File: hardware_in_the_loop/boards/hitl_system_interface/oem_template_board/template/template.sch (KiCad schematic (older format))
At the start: 35 parts, among them J1 CONN_02X03, U1 MCP2561-E_SN, U101 TPS560430YF, U2 ATMEGA16M1, Y1 Crystal_SMD

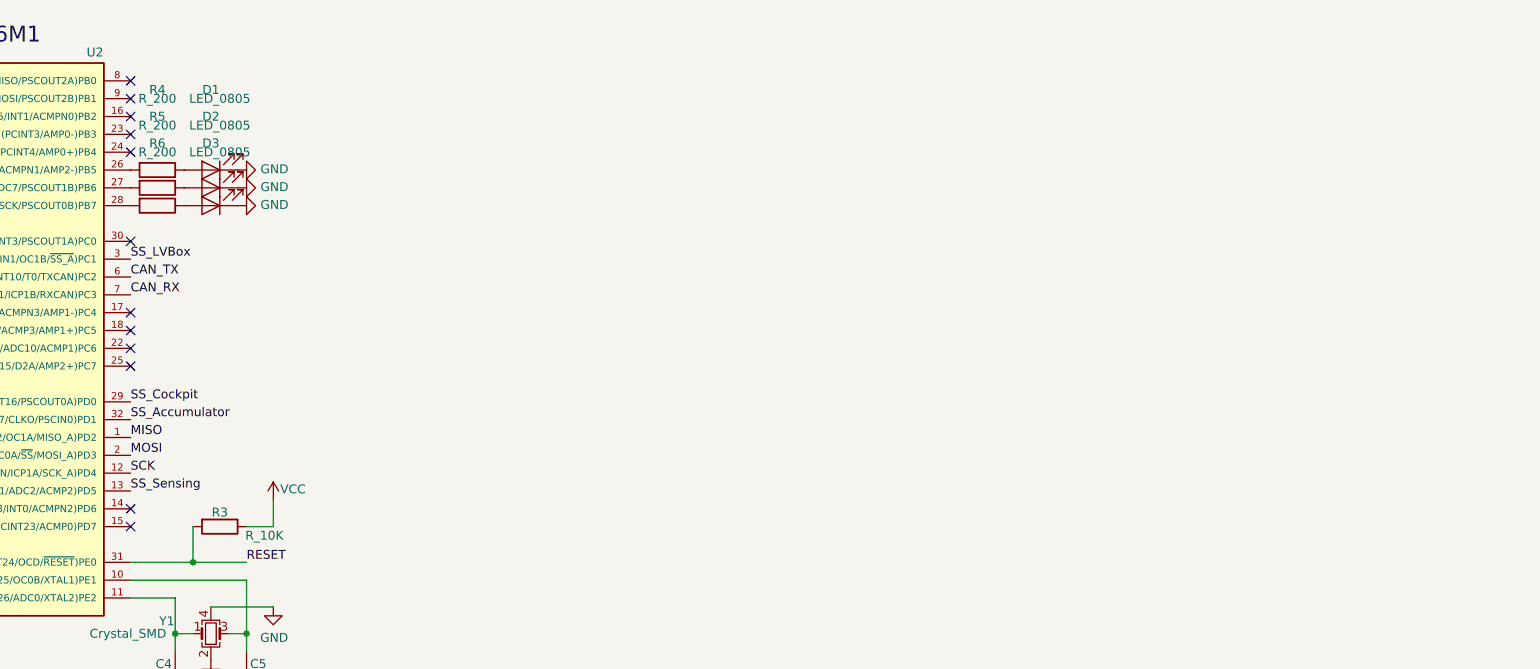
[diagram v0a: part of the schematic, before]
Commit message: Worked on USB_MicroB connections to FT232R
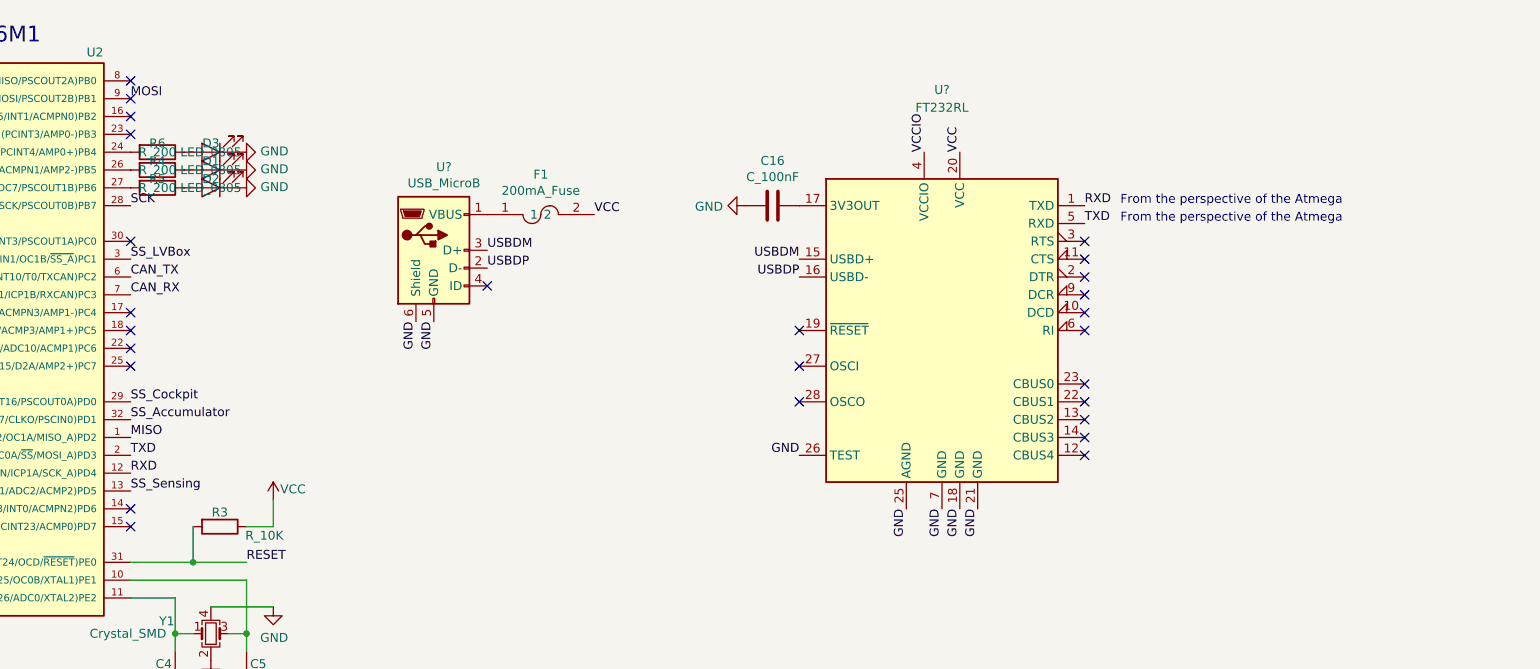
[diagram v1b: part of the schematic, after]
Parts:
- added C16: C_100nF, footprints:C_0603_1608Metric, symbol formula:C_100nF
- added F1: 200mA_Fuse, footprints:Fuse_1812, symbol formula:200mA_Fuse
- added U?: FT232RL, Package_SO:SSOP-28_5.3x10.2mm_P0.65mm, symbol formula:FT232RL
- added U?: USB_MicroB, Connectors_USB:USB_Micro-B_Molex-105017-0001, symbol formula:USB_MicroB
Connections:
- net GND: now also C16.2, U?.18 (GND), U?.21 (GND), U?.25 (AGND), U?.26 (TEST), U?.5 (GND), U?.6 (Shield), U?.7 (GND)
- net MOSI: now also U2.9 ((PCINT1/MOSI/PSCOUT2B)PB1); no longer U2.2 ((PCINT19/TXD/TXLIN/OC0A/~SS~/MOSI_A)PD3)
- net SCK: now also U2.28 ((PCINT7/ADC4/SCK/PSCOUT0B)PB7); no longer U2.12 ((PCINT20/ADC1/RXD/RXLIN/ICP1A/SCK_A)PD4)
- net VCC: now also F1.2, U?.20 (VCC)
- net at U2.24 ((PCINT4/AMP0+)PB4): now also R6.2
- new net: C16.1, U?.17 (3V3OUT)
- new net: F1.1, U?.1 (VBUS)
- new net RXD: U2.12 ((PCINT20/ADC1/RXD/RXLIN/ICP1A/SCK_A)PD4), U?.1 (TXD)
- new net TXD: U2.2 ((PCINT19/TXD/TXLIN/OC0A/~SS~/MOSI_A)PD3), U?.5 (RXD)
- new net USBDM: U?.15 (USBD+), U?.3 (D+)
- new net USBDP: U?.16 (USBD-), U?.2 (D-)
- new net VCCIO: U?.4 (VCCIO)
- no-connect marks 14 -> 28
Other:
- note added: "From the perspective of the Atmega"
- moved on the sheet: D3, R6
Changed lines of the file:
@@
 Text Label 3650 3000 0    50   ~ 0
 MISO
-Text Label 3650 3100 0    50   ~ 0
+Text Label 3650 1100 0    50   ~ 0
 MOSI
 Text Label 3650 3200 0    50   ~ 0
-SCK
+RXD
 Text Label 4300 3700 0    50   ~ 0
 RESET
@@
 U 1 1 5F9FF68D
 P 4100 1500
-F 0 "D1" H 4100 1050 50  0000 C CNN
-F 1 "LED_0805" H 4050 1100 50  0000 C CNN
+F 0 "D1" H 4100 1450 50  0000 C CNN
+F 1 "LED_0805" H 4100 1500 50  0000 C CNN
 F 2 "footprints:LED_0805_OEM" H 4000 1500 50  0001 C CNN
 F 3 "http://www.osram-os.com/Graphics/XPic9/00078860_0.pdf" H 4100 1600 50  0001 C CNN
@@
 U 1 1 5FA08DE6
 P 3800 1500
-F 0 "R4" V 3350 1500 50  0000 C CNN
-F 1 "R_200" V 3400 1500 50  0000 C CNN
+F 0 "R4" V 3750 1500 50  0000 C CNN
+F 1 "R_200" V 3800 1500 50  0000 C CNN
 F 2 "footprints:R_0805_OEM" H 3730 1500 50  0001 C CNN
 F 3 "https://www.seielect.com/Catalog/SEI-RMCF_RMCP.pdf" H 3880 1500 50  0001 C CNN
@@
 U 1 1 5FA12380
 P 4100 1600
-F 0 "D2" H 4100 1200 50  0000 C CNN
-F 1 "LED_0805" H 4050 1250 50  0000 C CNN
+F 0 "D2" H 4100 1550 50  0000 C CNN
+F 1 "LED_0805" H 4100 1600 50  0000 C CNN
 F 2 "footprints:LED_0805_OEM" H 4000 1600 50  0001 C CNN
 F 3 "http://www.osram-os.com/Graphics/XPic9/00078860_0.pdf" H 4100 1700 50  0001 C CNN
@@
 U 1 1 5FA12389
 P 3800 1600
-F 0 "R5" V 3400 1600 50  0000 C CNN
-F 1 "R_200" V 3450 1600 50  0000 C CNN
+F 0 "R5" V 3750 1600 50  0000 C CNN
+F 1 "R_200" V 3800 1600 50  0000 C CNN
 F 2 "footprints:R_0805_OEM" H 3730 1600 50  0001 C CNN
 F 3 "https://www.seielect.com/Catalog/SEI-RMCF_RMCP.pdf" H 3880 1600 50  0001 C CNN
@@
 $EndComp
 $Comp
-L formula:LED_0805 D3
-U 1 1 5FA147E9
-P 4100 1700
-F 0 "D3" H 4100 1350 50  0000 C CNN
-F 1 "LED_0805" H 4050 1400 50  0000 C CNN
-F 2 "footprints:LED_0805_OEM" H 4000 1700 50  0001 C CNN
-F 3 "http://www.osram-os.com/Graphics/XPic9/00078860_0.pdf" H 4100 1800 50  0001 C CNN
-F 4 "DK" H 4100 1700 60  0001 C CNN "MFN"
-F 5 "475-1410-1-ND" H 4100 1700 60  0001 C CNN "MPN"
-F 6 "https://www.digikey.com/products/en?keywords=475-1410-1-ND" H 4500 2200 60  0001 C CNN "PurchasingLink"
-	1    4100 1700
-	-1   0    0    1
-$EndComp
-$Comp
 L formula:R_200 R6
 U 1 1 5FA147F2
-P 3800 1700
-F 0 "R6" V 3450 1700 50  0000 C CNN
-F 1 "R_200" V 3500 1700 50  0000 C CNN
-F 2 "footprints:R_0805_OEM" H 3730 1700 50  0001 C CNN
-F 3 "https://www.seielect.com/Catalog/SEI-RMCF_RMCP.pdf" H 3880 1700 50  0001 C CNN
-F 4 "DK" H 3800 1700 60  0001 C CNN "MFN"
-F 5 "RMCF0805JT200RCT-ND" H 3800 1700 60  0001 C CNN "MPN"
-F 6 "https://www.digikey.com/products/en?keywords=RMCF0805JT200RCT-ND" H 4280 2100 60  0001 C CNN "PurchasingLink"
-	1    3800 1700
+P 3800 1400
+F 0 "R6" V 3750 1400 50  0000 C CNN
+F 1 "R_200" V 3800 1400 50  0000 C CNN
+F 2 "footprints:R_0805_OEM" H 3730 1400 50  0001 C CNN
+F 3 "https://www.seielect.com/Catalog/SEI-RMCF_RMCP.pdf" H 3880 1400 50  0001 C CNN
+F 4 "DK" H 3800 1400 60  0001 C CNN "MFN"
+F 5 "RMCF0805JT200RCT-ND" H 3800 1400 60  0001 C CNN "MPN"
+F 6 "https://www.digikey.com/products/en?keywords=RMCF0805JT200RCT-ND" H 4280 1800 60  0001 C CNN "PurchasingLink"
+	1    3800 1400
 	0    1    1    0
 $EndComp
@@
 L power:GND #PWR021
 U 1 1 5FA147F8
-P 4250 1700
-F 0 "#PWR021" H 4250 1450 50  0001 C CNN
-F 1 "GND" V 4255 1572 50  0000 R CNN
-F 2 "" H 4250 1700 50  0001 C CNN
-F 3 "" H 4250 1700 50  0001 C CNN
-	1    4250 1700
+P 4250 1400
+F 0 "#PWR021" H 4250 1150 50  0001 C CNN
+F 1 "GND" V 4255 1272 50  0000 R CNN
+F 2 "" H 4250 1400 50  0001 C CNN
+F 3 "" H 4250 1400 50  0001 C CNN
+	1    4250 1400
 	0    -1   -1   0
 $EndComp
@@
 NoConn ~ 3650 1200
 NoConn ~ 3650 1300
-NoConn ~ 3650 1400
-NoConn ~ 3650 1900
 NoConn ~ 3650 2300
 NoConn ~ 3650 2400
@@
 NoConn ~ 3650 3400
 NoConn ~ 3650 3500
+$Comp
+L formula:LED_0805 D3
+U 1 1 5FA147E9
+P 4100 1400
+F 0 "D3" H 4100 1350 50  0000 C CNN
+F 1 "LED_0805" H 4100 1400 50  0000 C CNN
+F 2 "footprints:LED_0805_OEM" H 4000 1400 50  0001 C CNN
+F 3 "http://www.osram-os.com/Graphics/XPic9/00078860_0.pdf" H 4100 1500 50  0001 C CNN
+F 4 "DK" H 4100 1400 60  0001 C CNN "MFN"
+F 5 "475-1410-1-ND" H 4100 1400 60  0001 C CNN "MPN"
+F 6 "https://www.digikey.com/products/en?keywords=475-1410-1-ND" H 4500 1900 60  0001 C CNN "PurchasingLink"
+	1    4100 1400
+	-1   0    0    1
+$EndComp
+Text Label 3650 3100 0    50   ~ 0
+TXD
+Text Label 3650 1700 0    50   ~ 0
+SCK
+NoConn ~ 3650 1900
+Text Label 9000 1800 0    50   ~ 0
+TXD
+Text Label 9000 1700 0    50   ~ 0
+RXD
+Text Notes 9200 1700 0    50   ~ 0
+From the perspective of the Atmega
+Text Notes 9200 1800 0    50   ~ 0
+From the perspective of the Atmega
+NoConn ~ 9000 1900
+NoConn ~ 9000 2000
+Text Label 8000 3400 3    50   ~ 0
+GND
+Text Label 8200 3400 3    50   ~ 0
+GND
+Text Label 8300 3400 3    50   ~ 0
+GND
+Text Label 8400 3400 3    50   ~ 0
+GND
+Text Label 7400 3100 2    50   ~ 0
+GND
+NoConn ~ 9000 2700
+NoConn ~ 9000 2800
+NoConn ~ 9000 2900
+NoConn ~ 9000 3000
+NoConn ~ 9000 3100
+NoConn ~ 9000 2400
+NoConn ~ 9000 2300
+NoConn ~ 9000 2200
+NoConn ~ 9000 2100
+$Comp
+L formula:C_100nF C16
+U 1 1 5FA17A78
+P 7250 1700
+F 0 "C16" V 6998 1700 50  0000 C CNN
+F 1 "C_100nF" V 7089 1700 50  0000 C CNN
+F 2 "footprints:C_0603_1608Metric" H 7288 1550 50  0001 C CNN
+F 3 "http://www.samsungsem.com/kr/support/product-search/mlcc/CL10A475KQ8NNNC.jsp" H 7275 1800 50  0001 C CNN
+F 4 "DK" H 7250 1700 60  0001 C CNN "MFN"
+F 5 "1276-6717-1-ND" H 7250 1700 60  0001 C CNN "MPN"
+F 6 "https://www.digikey.com/product-detail/en/samsung-electro-mechanics/CL10B104KA8WPNC/1276-6717-1-ND/5961576" H 7675 2200 60  0001 C CNN "PurchasingLink"
+	1    7250 1700
+	0    1    1    0
+$EndComp
+$Comp
+L power:GND #PWR?
+U 1 1 5FA19E14
+P 7100 1700
+F 0 "#PWR?" H 7100 1450 50  0001 C CNN
+F 1 "GND" V 7105 1572 50  0000 R CNN
+F 2 "" H 7100 1700 50  0001 C CNN
+F 3 "" H 7100 1700 50  0001 C CNN
+	1    7100 1700
+	0    1    1    0
+$EndComp
+$Comp
+L formula:USB_MicroB U?
+U 1 1 5FA24431
+P 5350 1950
+F 0 "U?" H 5407 2417 50  0000 C CNN
+F 1 "USB_MicroB" H 5407 2326 50  0000 C CNN
+F 2 "Connectors_USB:USB_Micro-B_Molex-105017-0001" H 5300 2300 50  0001 C CNN
+F 3 "https://www.molex.com/pdm_docs/sd/1050170001_sd.pdf" H 5300 2300 50  0001 C CNN
+F 4 "DK" H 5600 1700 50  0001 C CNN "MFN"
+F 5 "WM1399CT-ND" H 5700 1800 50  0001 C CNN "MPN"
+F 6 "https://www.digikey.com/product-detail/en/molex-llc/1050170001/WM1399CT-ND/2350885" H 5800 1900 50  0001 C CNN "PurchasingLink"
+	1    5350 1950
+	1    0    0    -1
+$EndComp
+Text Label 5350 2350 3    50   ~ 0
+GND
+Text Label 5250 2350 3    50   ~ 0
+GND
+NoConn ~ 5650 2150
+$Comp
+L formula:FT232RL U?
+U 1 1 5F9FAF59
+P 8200 2400
+F 0 "U?" H 8200 3750 50  0000 C CNN
+F 1 "FT232RL" H 8200 3650 50  0000 C CNN
+F 2 "Package_SO:SSOP-28_5.3x10.2mm_P0.65mm" H 9300 1500 50  0001 C CNN
+F 3 "https://www.ftdichip.com/Support/Documents/DataSheets/ICs/DS_FT232R.pdf" H 8200 2400 50  0001 C CNN
+F 4 "https://www.digikey.com/product-detail/en/ftdi-future-technology-devices-international-ltd/FT232RL-REEL/768-1007-1-ND/1836402" H 8200 2400 50  0001 C CNN "Purchasing Link"
+F 5 "768-1007-1-ND" H 8200 2400 50  0001 C CNN "Part Number (DK)"
+	1    8200 2400
+	1    0    0    -1
+$EndComp
+Text Label 8300 1400 1    50   ~ 0
+VCC
+Text Label 7400 2000 2    50   ~ 0
+USBDM
+Text Label 7400 2100 2    50   ~ 0
+USBDP
+Text Label 8100 1400 1    50   ~ 0
+VCCIO
+Text Label 5650 1950 0    50   ~ 0
+USBDM
+Text Label 5650 2050 0    50   ~ 0
+USBDP
+NoConn ~ 7400 2400
+NoConn ~ 7400 2600
+NoConn ~ 7400 2800
+$Comp
+L formula:200mA_Fuse F1
+U 1 1 5FA32B43
+P 5950 1750
+F 0 "F1" H 5950 1975 50  0000 C CNN
+F 1 "200mA_Fuse" H 5950 1884 50  0000 C CNN
+F 2 "footprints:Fuse_1812" H 5900 1750 50  0001 C CNN
+F 3 "https://www.belfuse.com/resources/CircuitProtection/datasheets/0ZCG%20Nov2016.pdf" H 5900 1750 50  0001 C CNN
+F 4 "507-1767-1-ND " H 6050 2000 50  0001 C CNN "MPN"
+F 5 "https://www.digikey.com/product-detail/en/bel-fuse-inc/0ZCG0110AF2C/507-1767-1-ND/4156157" H 6150 2100 50  0001 C CNN "PurchasingLink"
+F 6 "DK" H 6250 2200 50  0001 C CNN "MFN"
+	1    5950 1750
+	1    0    0    -1
+$EndComp
+Text Label 6250 1750 0    50   ~ 0
+VCC
 $EndSCHEMATC
